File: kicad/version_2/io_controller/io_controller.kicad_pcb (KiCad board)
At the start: 2 copper layers, 99 x 98 mm, 20 parts

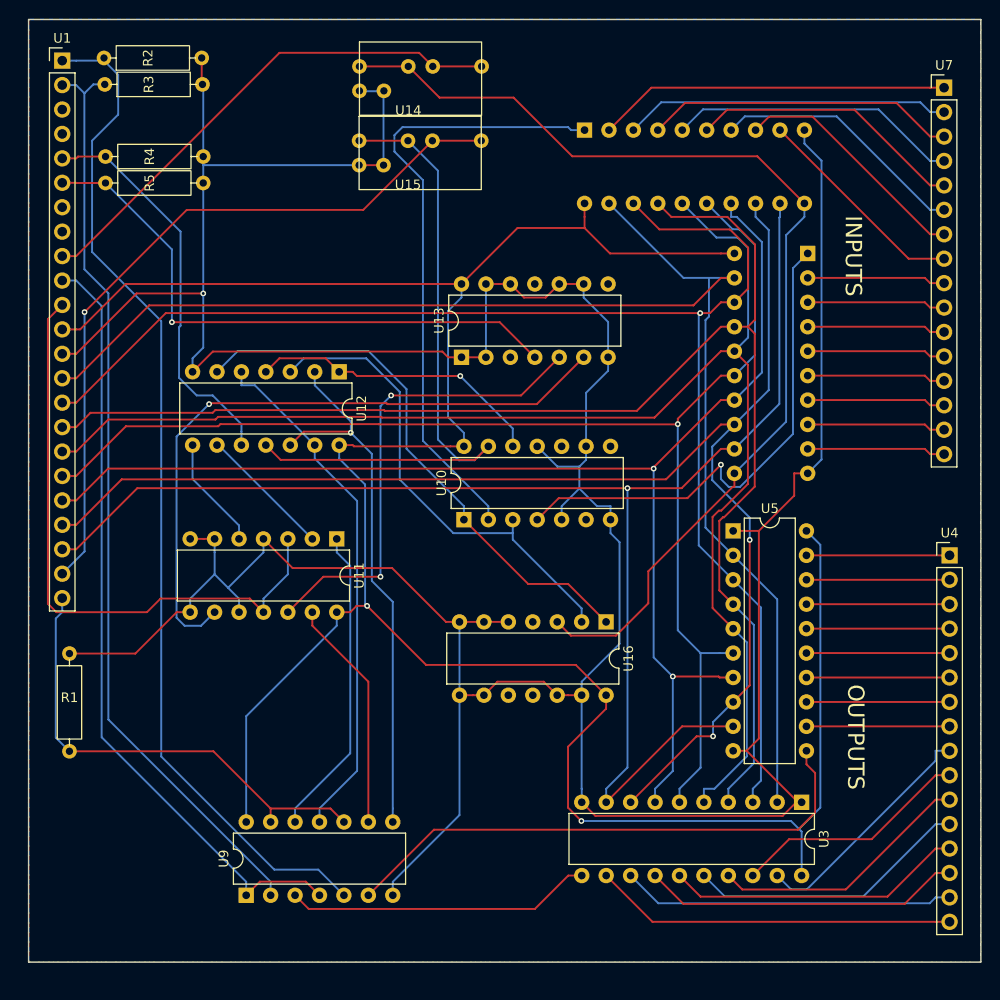
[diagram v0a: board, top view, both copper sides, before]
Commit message: Added connector on IO controller to support display
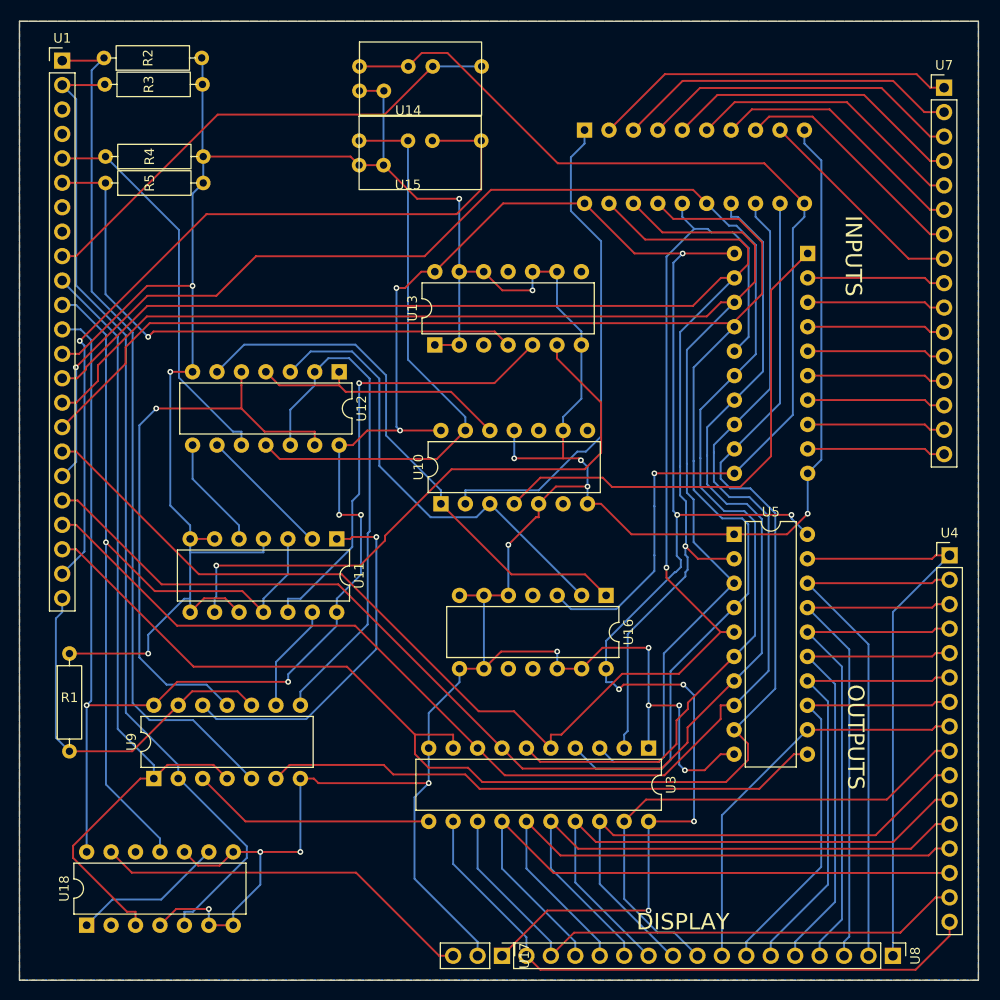
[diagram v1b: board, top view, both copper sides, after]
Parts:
- added U17: ~, Connector_PinHeader_2.54mm:PinHeader_1x03_P2.54mm_Vertical, F.Cu at (109.2, 116.8)
- added U18: ~, Package_DIP:DIP-14_W7.62mm, F.Cu at (66.0, 113.7)
- added U8: ~, Connector_PinHeader_2.54mm:PinHeader_1x16_P2.54mm_Vertical, F.Cu at (149.9, 116.8)
- moved U3 16.9 mm to (124.5, 95.2)
- moved U9 15.5 mm to (73.0, 98.4)
- moved U13 3.06 mm to (102.2, 53.3)
- moved U10 2.90 mm to (102.9, 69.8)
- moved U16 2.75 mm to (120.0, 79.4)
- moved U5 0.37 mm to (133.3, 73.0)
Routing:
- net Net-(U4-0): track 14.9 -> 59.0 mm
- net Net-(U4-1): track 14.9 -> 56.3 mm
- net Net-(U17-CLK): track 0.00 -> 40.0 mm
- net Net-(U4-2): track 14.9 -> 53.2 mm
- net Net-(U4-3): track 14.9 -> 51.0 mm
- net Net-(U1-GND): track 415.8 -> 450.0 mm, vias 1 -> 19
- net Net-(U4-4): track 14.9 -> 49.0 mm
- net Net-(U1-V+): track 260.5 -> 293.6 mm, vias 2 -> 13
- net Net-(U3-Q5): track 33.2 -> 65.9 mm
- net Net-(U3-Q1): track 24.8 -> 56.8 mm
- net Net-(U4-5): track 14.9 -> 46.9 mm
- net Net-(U3-Q4): track 31.1 -> 62.9 mm
- net Net-(U3-Q2): track 27.5 -> 58.7 mm
- net Net-(U3-Q3): track 29.5 -> 60.8 mm
- net Net-(U1-D4): track 140.4 -> 170.8 mm
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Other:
- board size 99 x 98 mm -> 99.7 x 99.7 mm
- board text added: "DISPLAY"
